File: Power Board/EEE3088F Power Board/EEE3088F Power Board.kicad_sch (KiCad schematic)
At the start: 6 parts, among them J1 Conn_02x16_Odd_Even, U1 INA219AxDCN

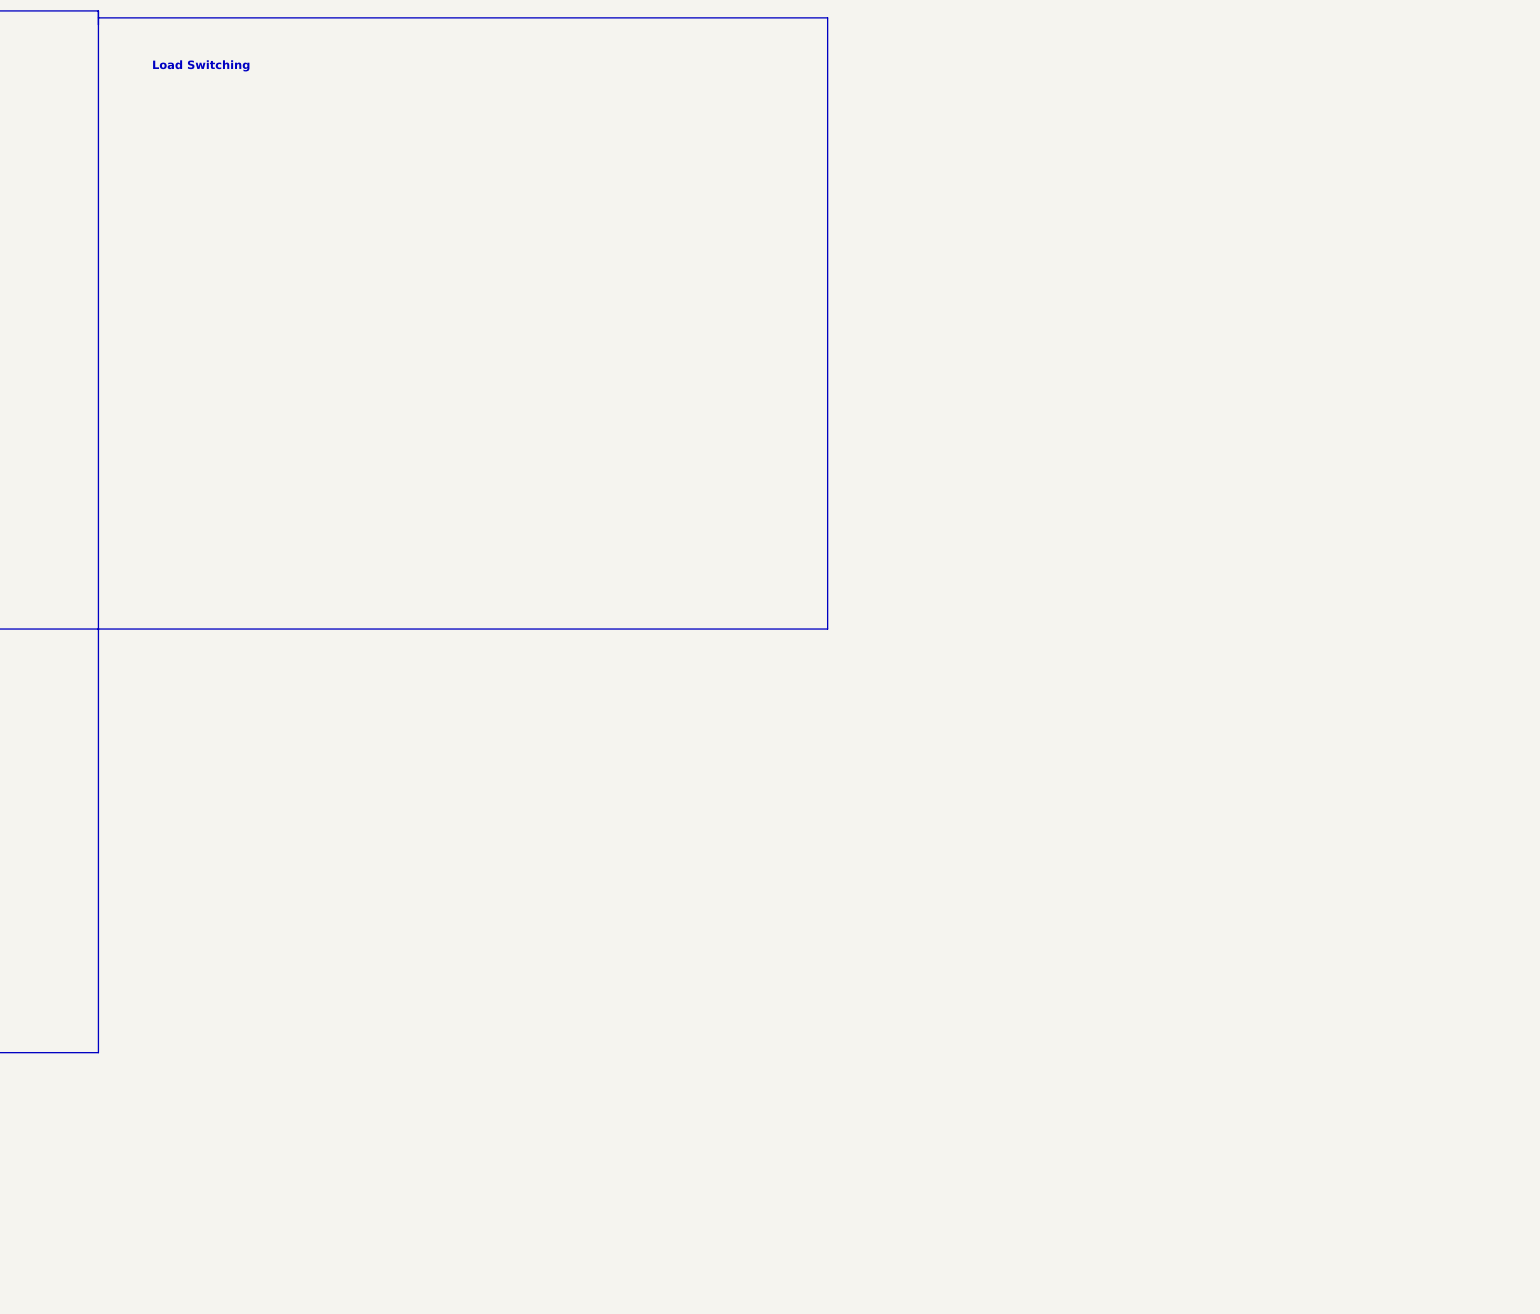
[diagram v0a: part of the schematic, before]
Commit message: added battery charging and started motor drivers
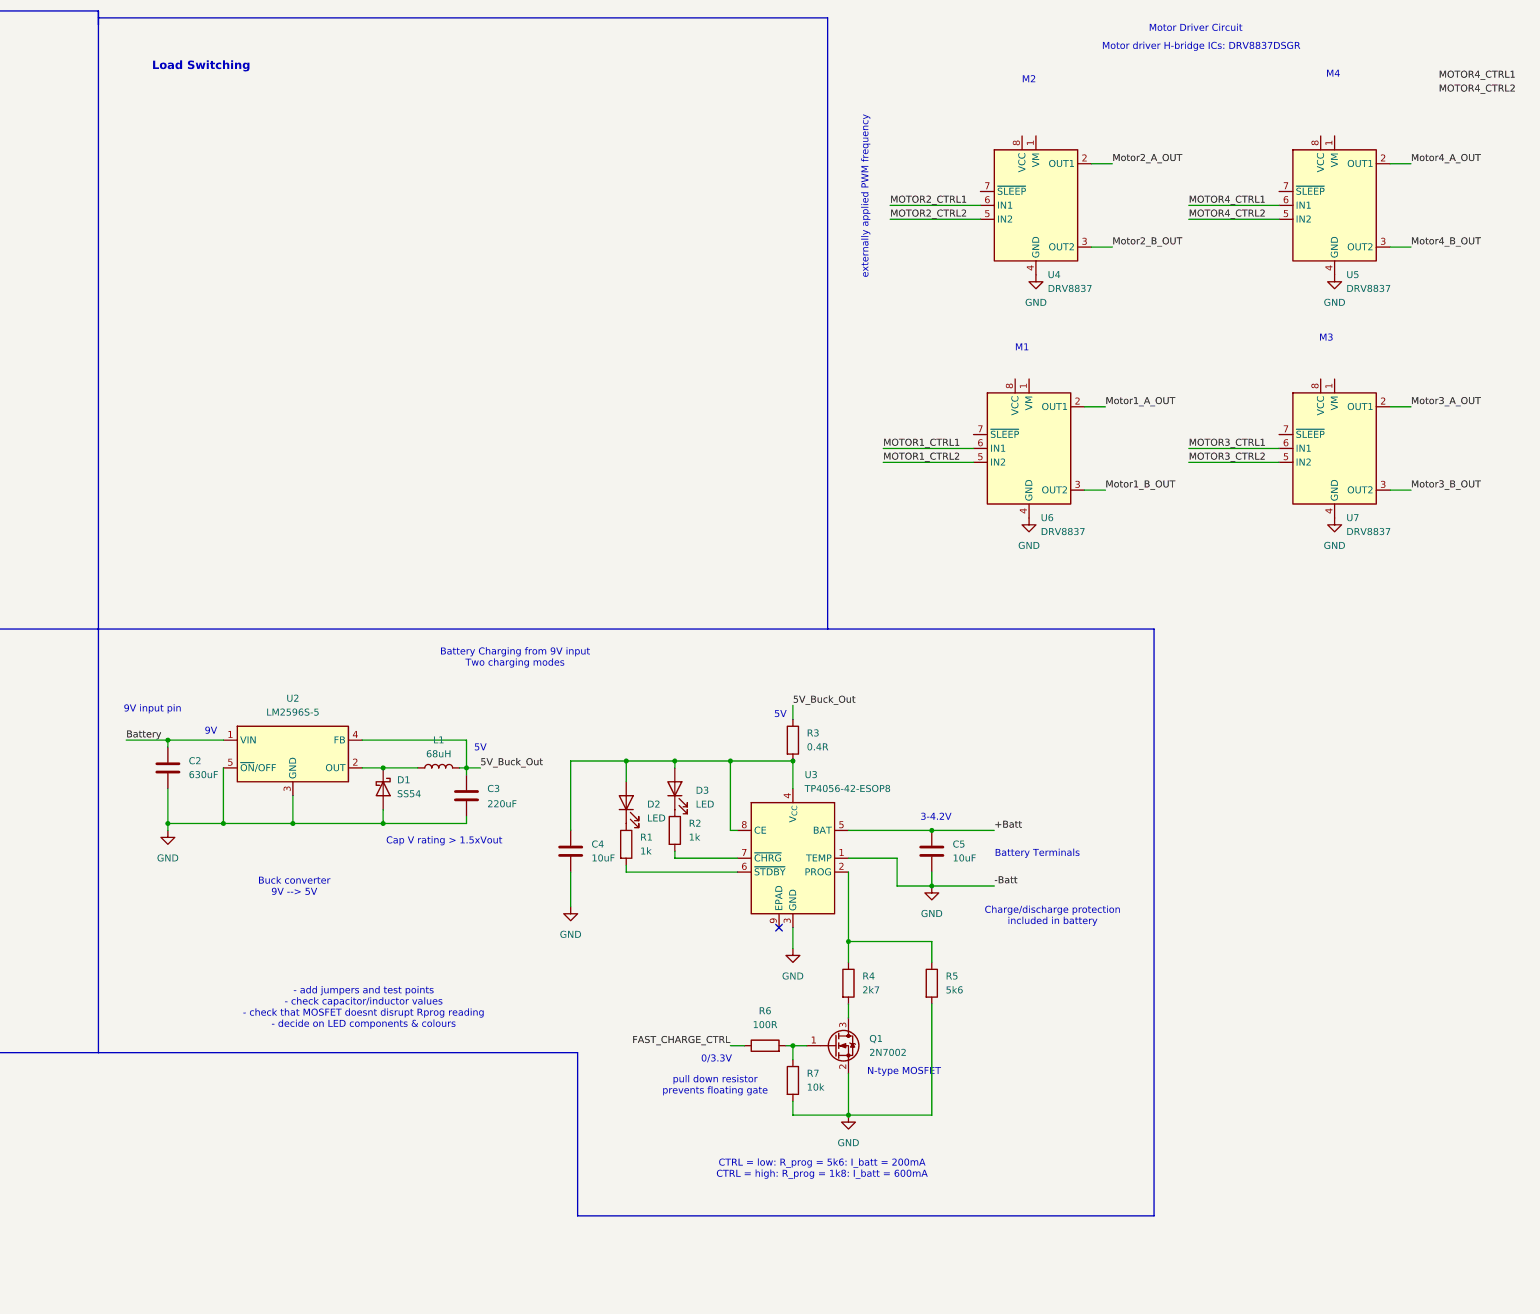
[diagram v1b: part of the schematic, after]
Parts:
- added C2: 630uF, symbol Device:C
- added C3: 220uF, symbol Device:C
- added C4, C5: 10uF, symbol Device:C
- added D1: SS54, Diode_SMD:D_SMA, symbol Diode:SS34
- added D2, D3: LED, symbol Device:LED
- added L1: 68uH, symbol Device:L
- added Q1: 2N7002, Package_TO_SOT_SMD:SOT-23, symbol Transistor_FET:2N7002
- added R1, R2: 1k, symbol Device:R
- added R3: 0.4R, symbol Device:R
- added R4: 2k7, 0805W8F2701T5E, symbol Device:R
- added R5: 5k6, 0805W8F5601T5E, symbol Device:R
- added R6: 100R, 1206W4F1000T5E, symbol Device:R
- added R7: 10k, symbol Device:R
- added U2: LM2596S-5, Package_TO_SOT_SMD:TO-263-5_TabPin3, symbol Regulator_Switching:LM2596S-5
- added U3: TP4056-42-ESOP8, Package_SO:SOIC-8-1EP_3.9x4.9mm_P1.27mm_EP2.41x3.3mm_ThermalVias, symbol Battery_Management:TP4056-42-ESOP8
- added U4, U5, U6, U7: DRV8837, Package_SON:WSON-8-1EP_2x2mm_P0.5mm_EP0.9x1.6mm, symbol Driver_Motor:DRV8837
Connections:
- net Battery: now also C2.1, U2.1 (VIN)
- net FAST_CHARGE_CTRL: now also R6.1
- net GND: now also C2.2, C3.2, C4.2, C5.2, D1.2 (A), Q1.2 (S), R5.2, R7.2, U2.3 (GND), U2.5 (~{ON}/OFF), U3.1 (TEMP), U3.3 (GND), U4.4 (GND), U4.9 (GND), U5.4 (GND), U5.9 (GND), U6.4 (GND), U6.9 (GND), U7.4 (GND), U7.9 (GND)
- net MOTOR1_CTRL1: now also U6.6 (IN1)
- net MOTOR1_CTRL2: now also U6.5 (IN2)
- net MOTOR2_CTRL1: now also U4.6 (IN1)
- net MOTOR2_CTRL2: now also U4.5 (IN2)
- net MOTOR3_CTRL1: now also U7.6 (IN1)
- net MOTOR3_CTRL2: now also U7.5 (IN2)
- net MOTOR4_CTRL1: now also U5.6 (IN1)
- net MOTOR4_CTRL2: now also U5.5 (IN2)
- net Motor2_A_OUT: now also U4.2 (OUT1)
- net Motor2_B_OUT: now also U4.3 (OUT2)
- net Motor4_A_OUT: now also U5.2 (OUT1)
- new net: R4.1, R5.1, U3.2 (PROG)
- new net: C4.1, D2.2 (A), D3.2 (A), R3.2, U3.4 (V_{CC}), U3.8 (CE)
- new net: R1.2, U3.6 (~{STDBY})
- new net: R2.2, U3.7 (~{CHRG})
- new net: Q1.1 (G), R6.2, R7.1
- new net: Q1.3 (D), R4.2
- new net: D3.1 (K), R2.1
- new net: D1.1 (K), L1.1, U2.2 (OUT)
- new net: D2.1 (K), R1.1
- new net +Batt: C5.1, U3.5 (BAT)
- new net 5V_Buck_Out: C3.1, L1.2, R3.1, U2.4 (FB)
- new net Motor1_A_OUT: U6.2 (OUT1)
- new net Motor1_B_OUT: U6.3 (OUT2)
- new net Motor3_A_OUT: U7.2 (OUT1)
- new net Motor3_B_OUT: U7.3 (OUT2)
- new net Motor4_B_OUT: U5.3 (OUT2)
- no-connect marks 0 -> 1
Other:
- note added: "- add jumpers and test points - check capacitor/inductor values - check that MOSFET doesnt disrupt Rprog reading - decide on LED components & colours"
- note added: "0/3.3V"
- note added: "3-4.2V"
- note added: "5V"
- note added: "9V"
- note added: "9V input pin"
- note added: "Battery Charging from 9V input Two charging modes"
- note added: "Battery Terminals"
- note added: "Buck converter 9V --> 5V"
- note added: "CTRL = low: R_prog = 5k6: I_batt = 200mA CTRL = high: R_prog = 1k8: I_batt = 600mA"
- note added: "Cap V rating > 1.5xVout"
- note added: "Charge/discharge protection included in battery"
- note added: "M1"
- note added: "M2"
- note added: "M3"
- note added: "M4"
- note added: "Motor Driver Circuit"
- note added: "Motor driver H-bridge ICs: DRV8837DSGR"
- note added: "N-type MOSFET"
- note added: "externally applied PWM frequency"
- note added: "pull down resistor prevents floating gate"

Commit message: finished motor driver circuit
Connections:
- net +Batt: now also U4.1 (VM), U5.1 (VM), U6.1 (VM), U7.1 (VM)
- net 3V3 Out: now also U4.7 (~{SLEEP}), U4.8 (VCC), U5.7 (~{SLEEP}), U5.8 (VCC), U6.7 (~{SLEEP}), U6.8 (VCC), U7.7 (~{SLEEP}), U7.8 (VCC)
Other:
- note added: "DRV8837"
- note added: "externally applied PWM frequency (from CNTRL pins)"
- note removed: "externally applied PWM frequency"
- moved on the sheet: C2, C3, C4, C5, D1, D2, D3, J1, L1, Q1, R1, R2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
